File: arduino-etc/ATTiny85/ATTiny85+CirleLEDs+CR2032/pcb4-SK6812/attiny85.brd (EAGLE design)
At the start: 40 x 40 mm, 13 parts, among them SW1 bat+, SW2 POWER

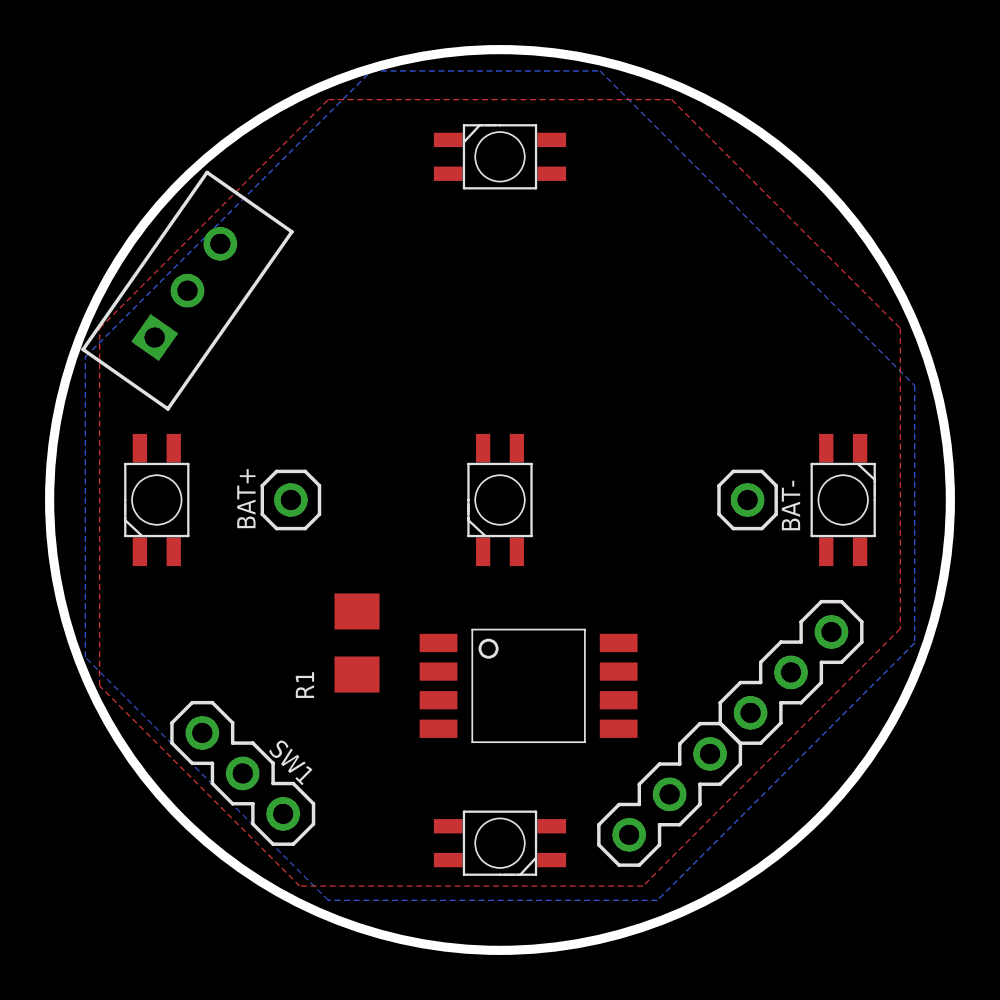
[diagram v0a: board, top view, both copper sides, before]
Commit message: FIX: pcb4-SK6812/
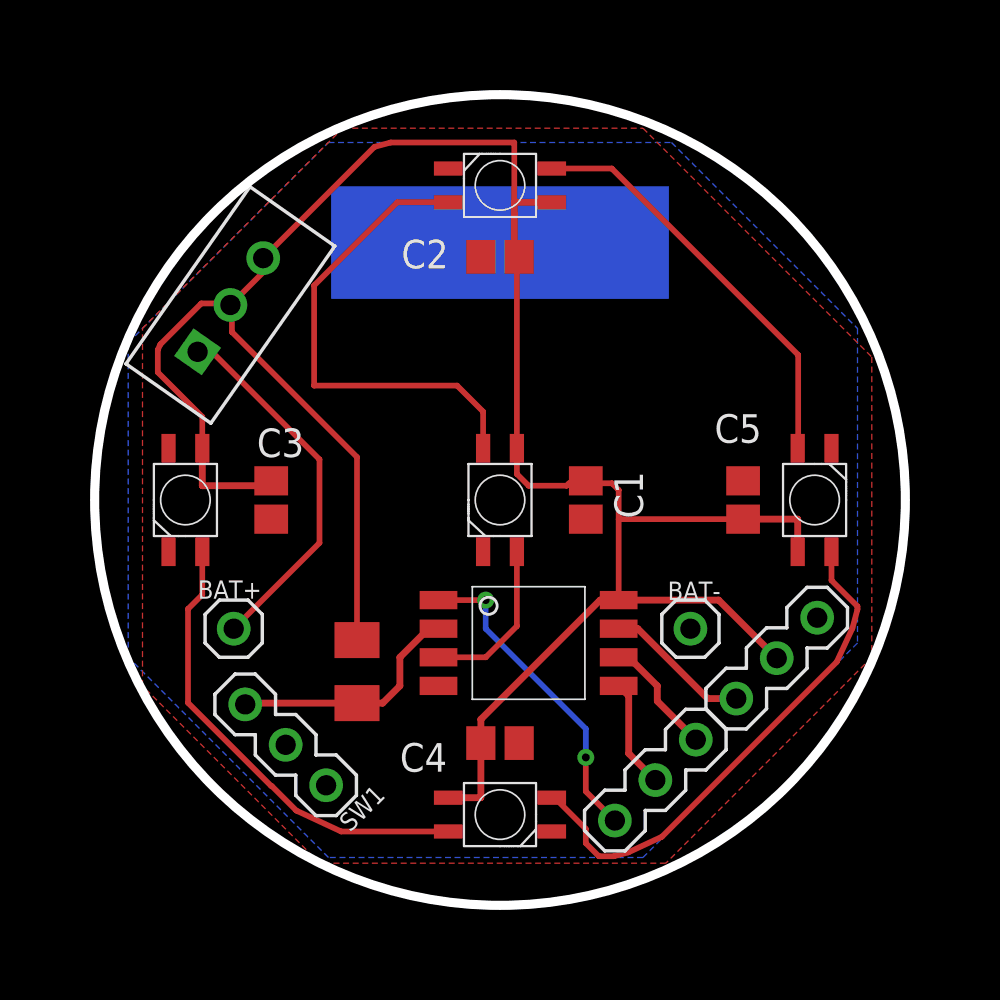
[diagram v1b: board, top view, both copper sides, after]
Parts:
- added C1, C2, C3, C4, C5: (no value), rcl:C2012
- added PAD33: PAD150X50, ytani1:PAD5X15
- moved BAT+ 6.25 mm to (32.6, 34.9)
- moved BAT- 6.25 mm to (52.9, 34.9)
- moved SW1 2.29 mm to (37.1, 28.9)
- moved SW2 2.01 mm to (33.0, 48.3)
- moved ATTINY85-1 1.91 mm to (47.0, 34.3)
- moved SK2 1.27 mm to (45.7, 54.6)
- moved SK3 1.27 mm to (59.7, 40.6)
- moved SK4 1.27 mm to (45.7, 26.7)
- moved SK5 1.27 mm to (31.8, 40.6)
- moved R1 1.27 mm to (39.4, 33.0)
- moved SV1 0.90 mm to (51.7, 27.3)
- moved SV2 0.90 mm to (57.1, 32.7)
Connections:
- net BAT+: now also C1.1, C2.1, C3.1, C4.1, C5.1
- net GND: now also C1.2, C2.2, C3.2, C4.2, C5.2
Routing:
- net BAT+: track 0.00 -> 105.0 mm
- net N$8: track 0.61 -> 23.0 mm
- net N$6: track 0.00 -> 21.5 mm
- net N$9: track 0.00 -> 20.7 mm
- net N$7: track 0.08 -> 18.5 mm
- net +3V3: track 0.00 -> 16.5 mm
- net N$4: track 0.00 -> 14.3 mm, vias 0 -> 2
- net PB3: track 0.00 -> 10.7 mm
- net N$1: track 0.00 -> 7.35 mm
- net N$2: track 0.00 -> 6.51 mm
- net N$3: track 0.00 -> 5.33 mm
- net N$5: track 0.00 -> 4.86 mm
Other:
- board size 40 x 40 mm -> 36 x 36 mm
